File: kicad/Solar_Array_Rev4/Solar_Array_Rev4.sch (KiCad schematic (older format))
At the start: 7 parts

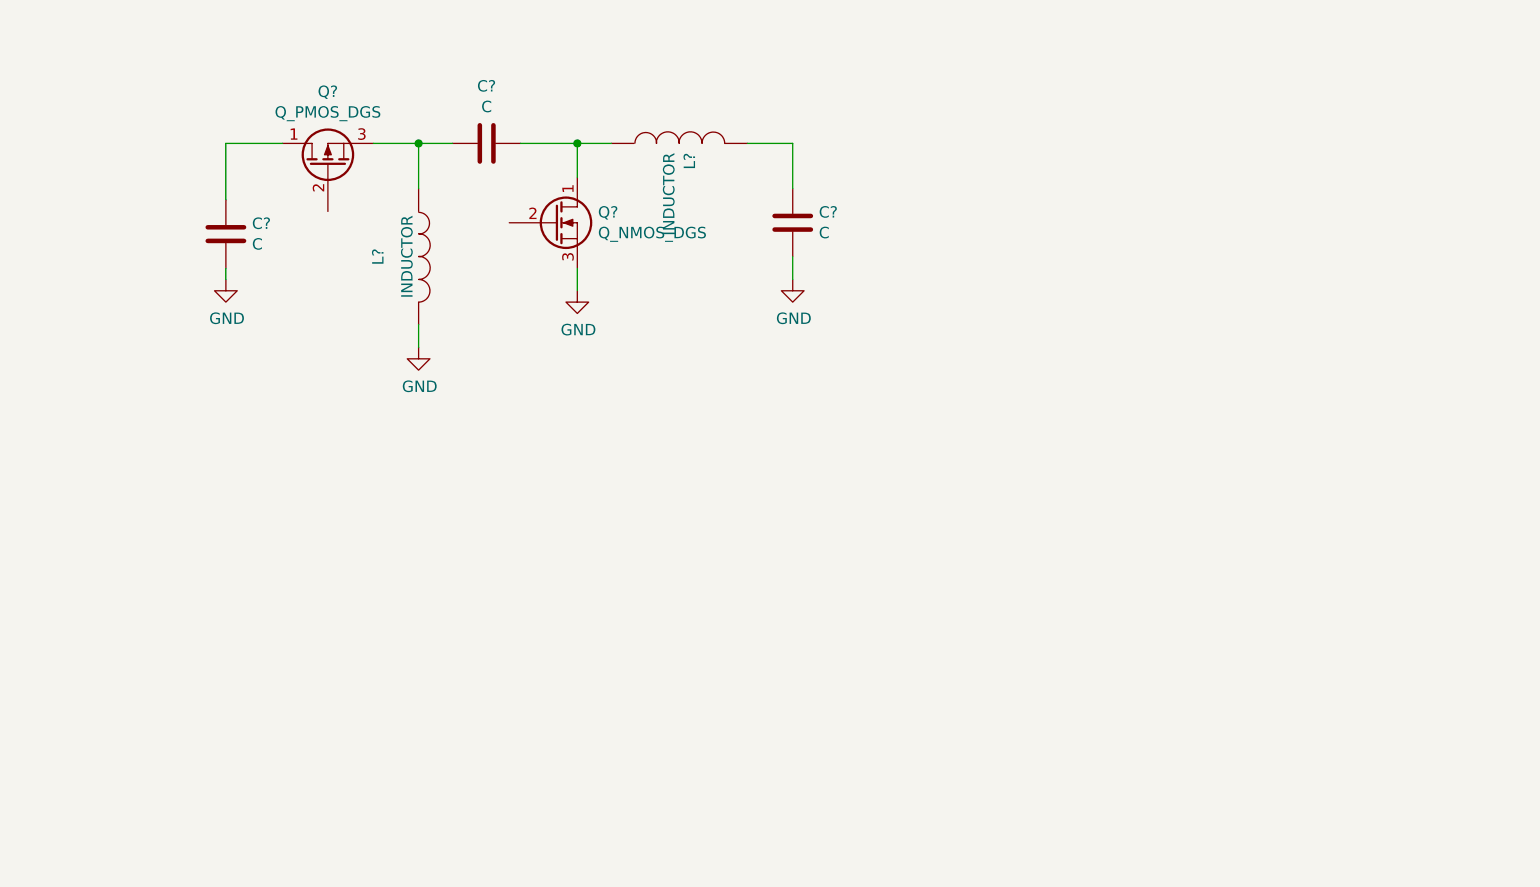
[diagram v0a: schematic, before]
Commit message: Created Schematics, Added Current Sense Circuitry -Created microcontroller schematic symbol -Created sense comparator schematic -Updated design with correct symbols -Added PV in/out -Calculated and selected --P-MOS --N-MOS --Check design docs for details
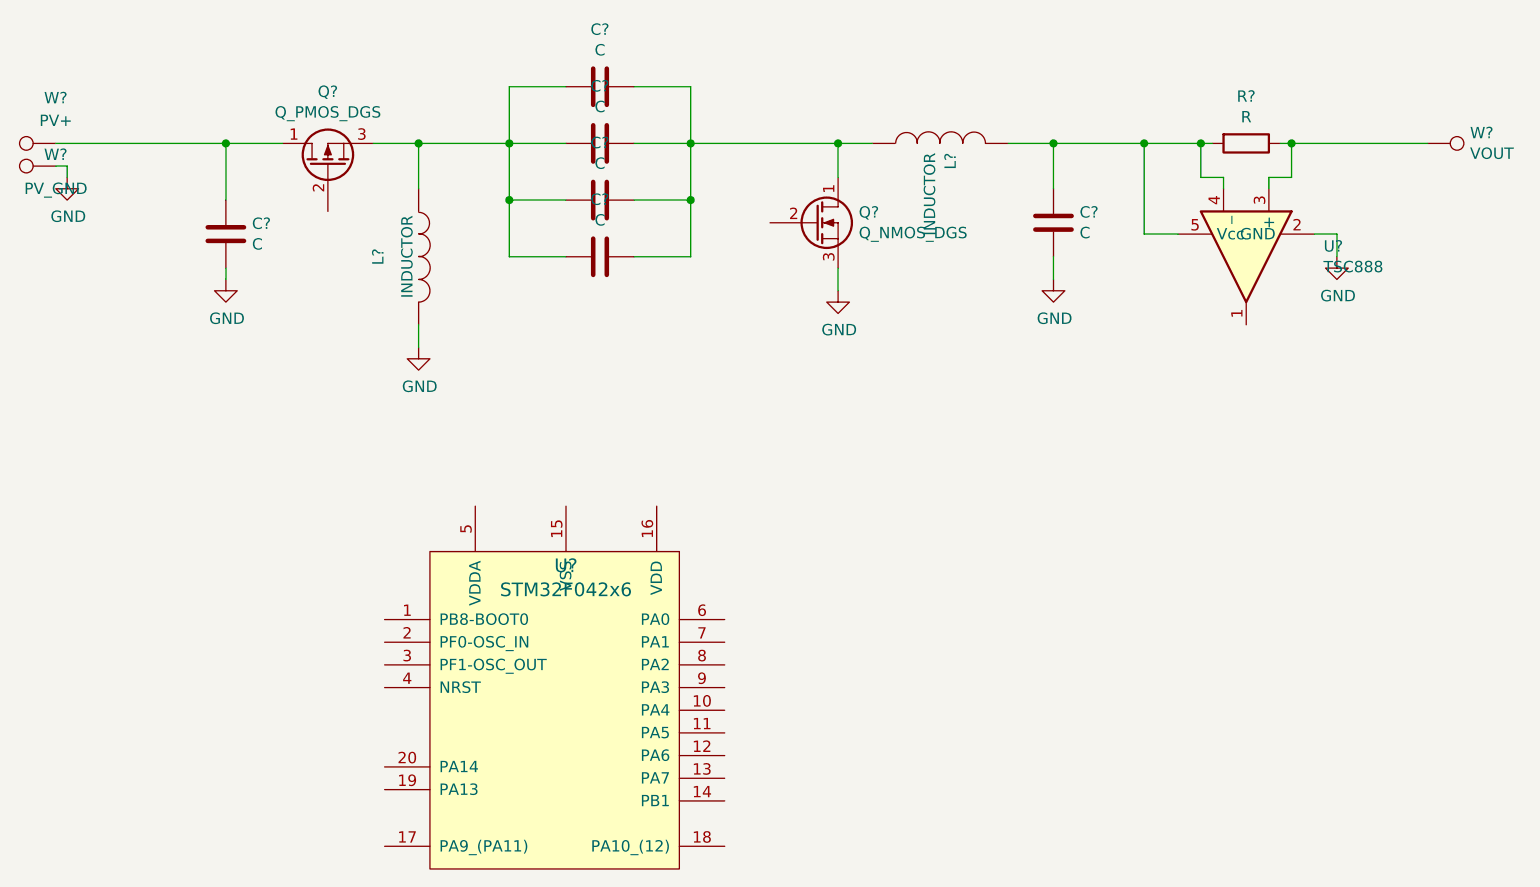
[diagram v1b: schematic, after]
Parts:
- added C? (x3): C, symbol C
- added R?: R, symbol R
- added U?: STM32F042x6, symbol STM32F042x6
- added U?: TSC888, symbol TSC888
- added W?: PV+, symbol TEST_1P
- added W?: PV_GND, symbol TEST_1P
- added W?: VOUT, symbol TEST_1P
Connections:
- net GND: now also U?.2 (GND), W?.1
- net at C?.1, L?.1, Q?.3 (S): now also C?.1, C?.1, C?.1
- net at C?.2, L?.1, Q?.1 (D): now also C?.2, C?.2, C?.2
- net at C?.1, L?.2: now also R?.2, U?.4 (_), U?.5 (Vcc)
- net at C?.1, Q?.1 (D): now also W?.1
- new net: R?.1, U?.3 (+), W?.1
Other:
- moved on the sheet: C?, L?, Q?

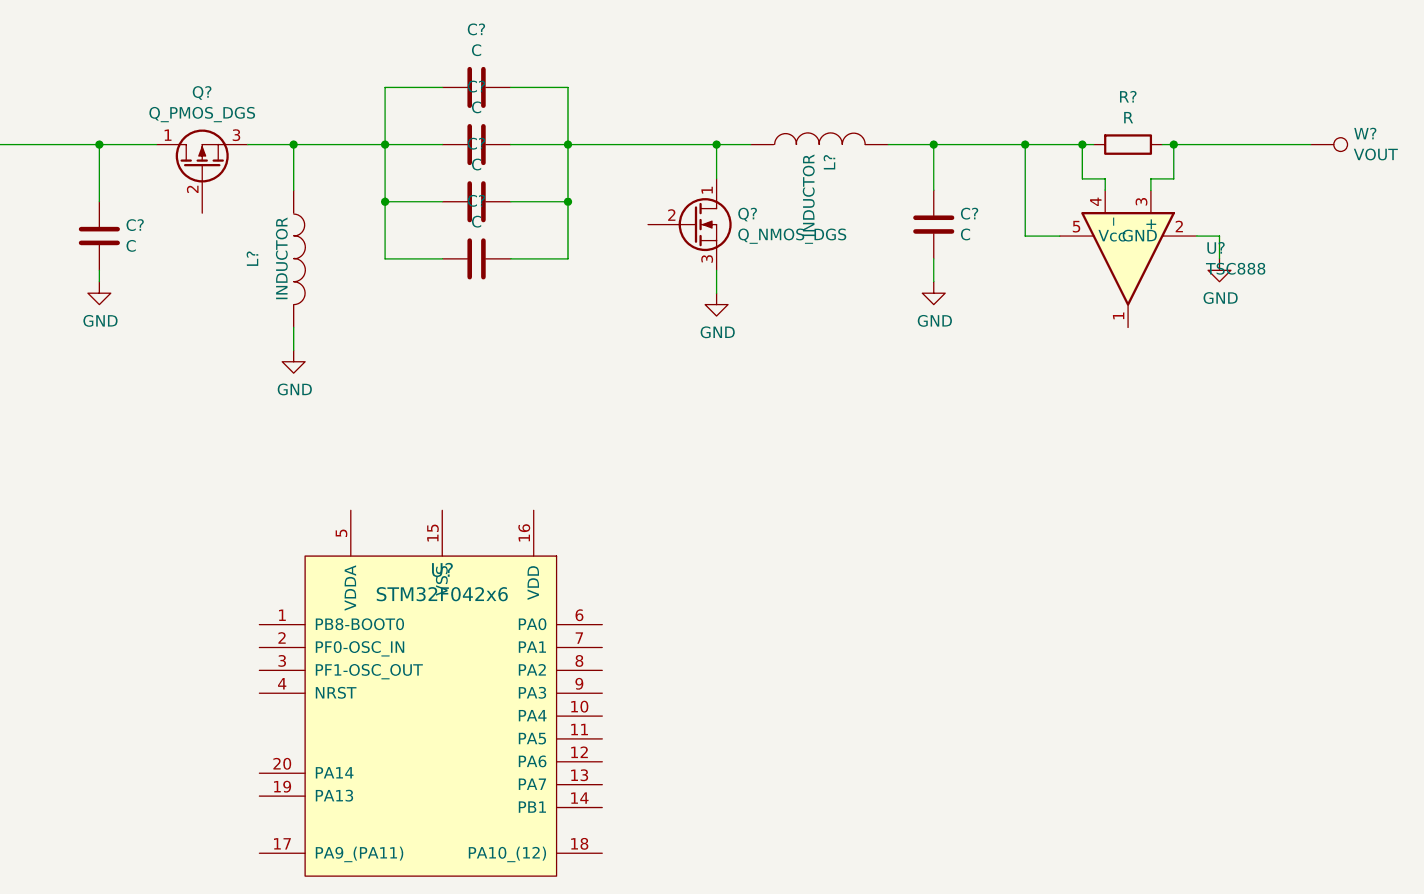
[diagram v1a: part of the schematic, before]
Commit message: Assigned Pin functions to ST microcontroller. -Found CAN TX/RX and assigned. -Found ADC in's for voltage/current sense. -Found TIM1 chn 1/3 for PWM control
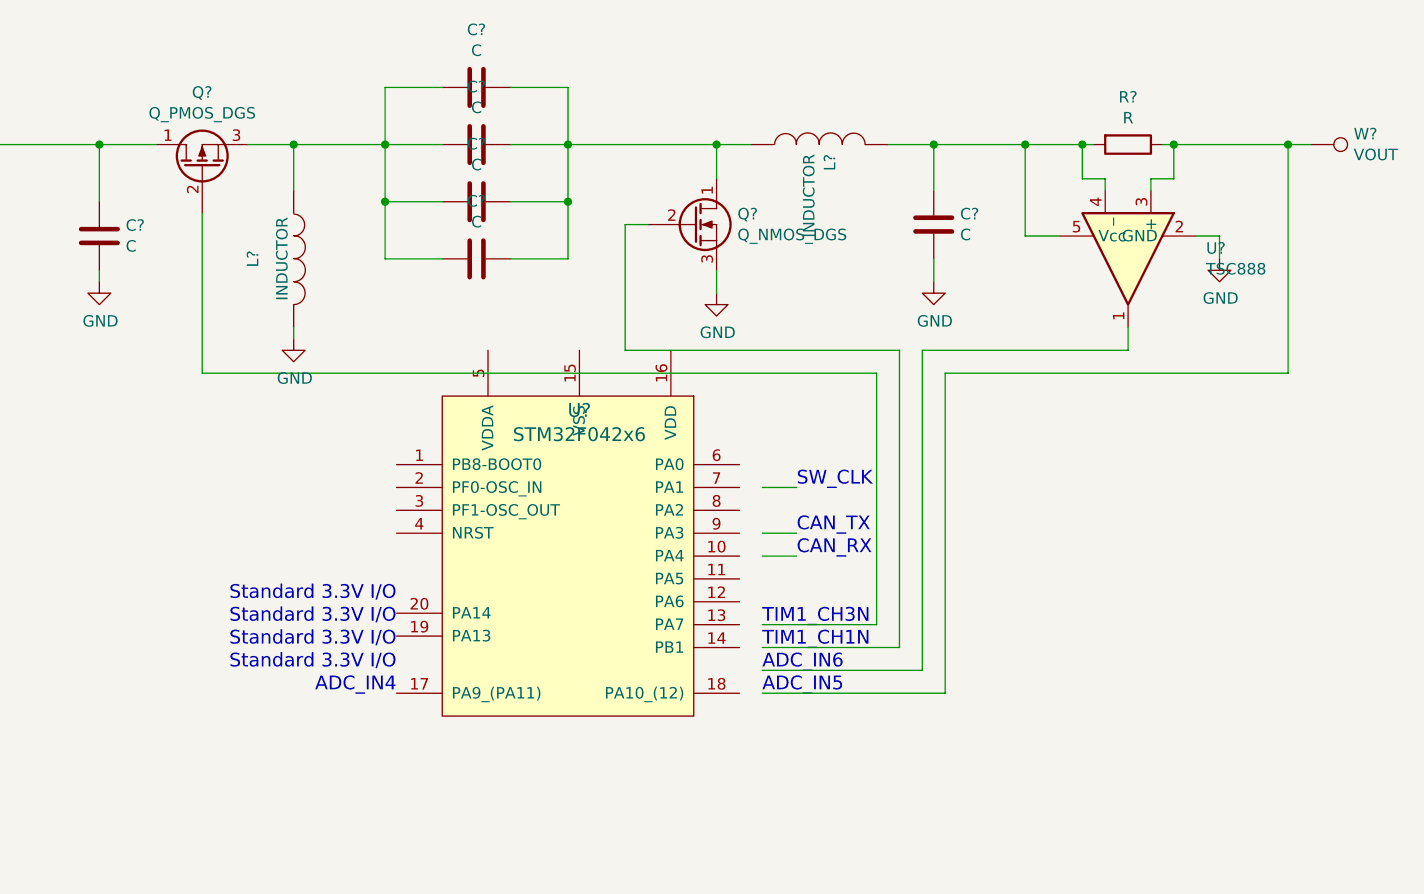
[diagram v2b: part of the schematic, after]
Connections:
- wire segments 33 -> 53
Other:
- note added: "ADC_IN4"
- note added: "ADC_IN5"
- note added: "ADC_IN6"
- note added: "CAN_RX"
- note added: "CAN_TX"
- note added: "SW_CLK"
- note added: "Standard 3.3V I/O"
- note added: "TIM1_CH1N"
- note added: "TIM1_CH3N"
- moved on the sheet: U?
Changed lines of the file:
@@
 L GND #PWR?
 U 1 1 57427E8E
-P 3550 3350
-F 0 "#PWR?" H 3550 3100 50  0001 C CNN
-F 1 "GND" H 3555 3177 50  0000 C CNN
-F 2 "" H 3550 3350 50  0000 C CNN
-F 3 "" H 3550 3350 50  0000 C CNN
-	1    3550 3350
+P 3550 3300
+F 0 "#PWR?" H 3550 3050 50  0001 C CNN
+F 1 "GND" H 3555 3127 50  0000 C CNN
+F 2 "" H 3550 3300 50  0000 C CNN
+F 3 "" H 3550 3300 50  0000 C CNN
+	1    3550 3300
 	1    0    0    -1
 $EndComp
@@
 L STM32F042x6 U?
 U 1 1 5748B95F
-P 4200 5100
-F 0 "U?" H 4200 5887 60  0000 C CNN
-F 1 "STM32F042x6" H 4200 5781 60  0000 C CNN
-F 2 "" H 4200 5100 60  0001 C CNN
-F 3 "" H 4200 5100 60  0001 C CNN
-	1    4200 5100
+P 4800 4400
+F 0 "U?" H 4800 5187 60  0000 C CNN
+F 1 "STM32F042x6" H 4800 5081 60  0000 C CNN
+F 2 "" H 4800 4400 60  0001 C CNN
+F 3 "" H 4800 4400 60  0001 C CNN
+	1    4800 4400
 	1    0    0    -1
 $EndComp
@@
 	2700 3000 2700 3050
 Wire Wire Line
-	3550 3250 3550 3350
-Wire Wire Line
 	5400 3000 5400 3100
 Wire Wire Line
@@
 	0    1    1    0
 $EndComp
+Connection ~ 7900 2450
+Wire Wire Line
+	5600 4250 5750 4250
+Wire Wire Line
+	5600 4150 5750 4150
+Text Notes 5750 4150 0    60   ~ 0
+CAN_TX
+Text Notes 5750 4250 0    60   ~ 0
+CAN_RX
+Text Notes 5750 3950 0    60   ~ 0
+SW_CLK
+Wire Wire Line
+	5600 3950 5750 3950
+Text Notes 4000 4450 2    60   ~ 0
+Standard 3.3V I/O
+Text Notes 4000 4550 2    60   ~ 0
+Standard 3.3V I/O
+Text Notes 4000 4650 2    60   ~ 0
+Standard 3.3V I/O
+Text Notes 4000 4750 2    60   ~ 0
+Standard 3.3V I/O
+Text Notes 4000 4850 2    60   ~ 0
+ADC_IN4
+Text Notes 5600 4650 0    60   ~ 0
+TIM1_CH1N
+Text Notes 5600 4550 0    60   ~ 0
+TIM1_CH3N
+Text Notes 5600 4850 0    60   ~ 0
+ADC_IN5
+Wire Wire Line
+	5600 4650 6200 4650
+Wire Wire Line
+	6200 4650 6200 3350
+Wire Wire Line
+	6200 3350 5000 3350
+Wire Wire Line
+	5000 3350 5000 2800
+Wire Wire Line
+	5000 2800 5100 2800
+Wire Wire Line
+	5600 4550 6100 4550
+Wire Wire Line
+	6100 4550 6100 3450
+Wire Wire Line
+	6100 3450 3150 3450
+Wire Wire Line
+	3150 3450 3150 2750
+Wire Wire Line
+	3550 3250 3550 3300
+Text Notes 5600 4750 0    60   ~ 0
+ADC_IN6
+Wire Wire Line
+	6300 4750 6300 3350
+Wire Wire Line
+	6300 3350 7200 3350
+Wire Wire Line
+	6300 4750 5600 4750
+Wire Wire Line
+	7200 3350 7200 3250
+Wire Wire Line
+	5600 4850 6400 4850
+Wire Wire Line
+	6400 4850 6400 3450
+Wire Wire Line
+	6400 3450 7900 3450
+Wire Wire Line
+	7900 3450 7900 2450
 $EndSCHEMATC

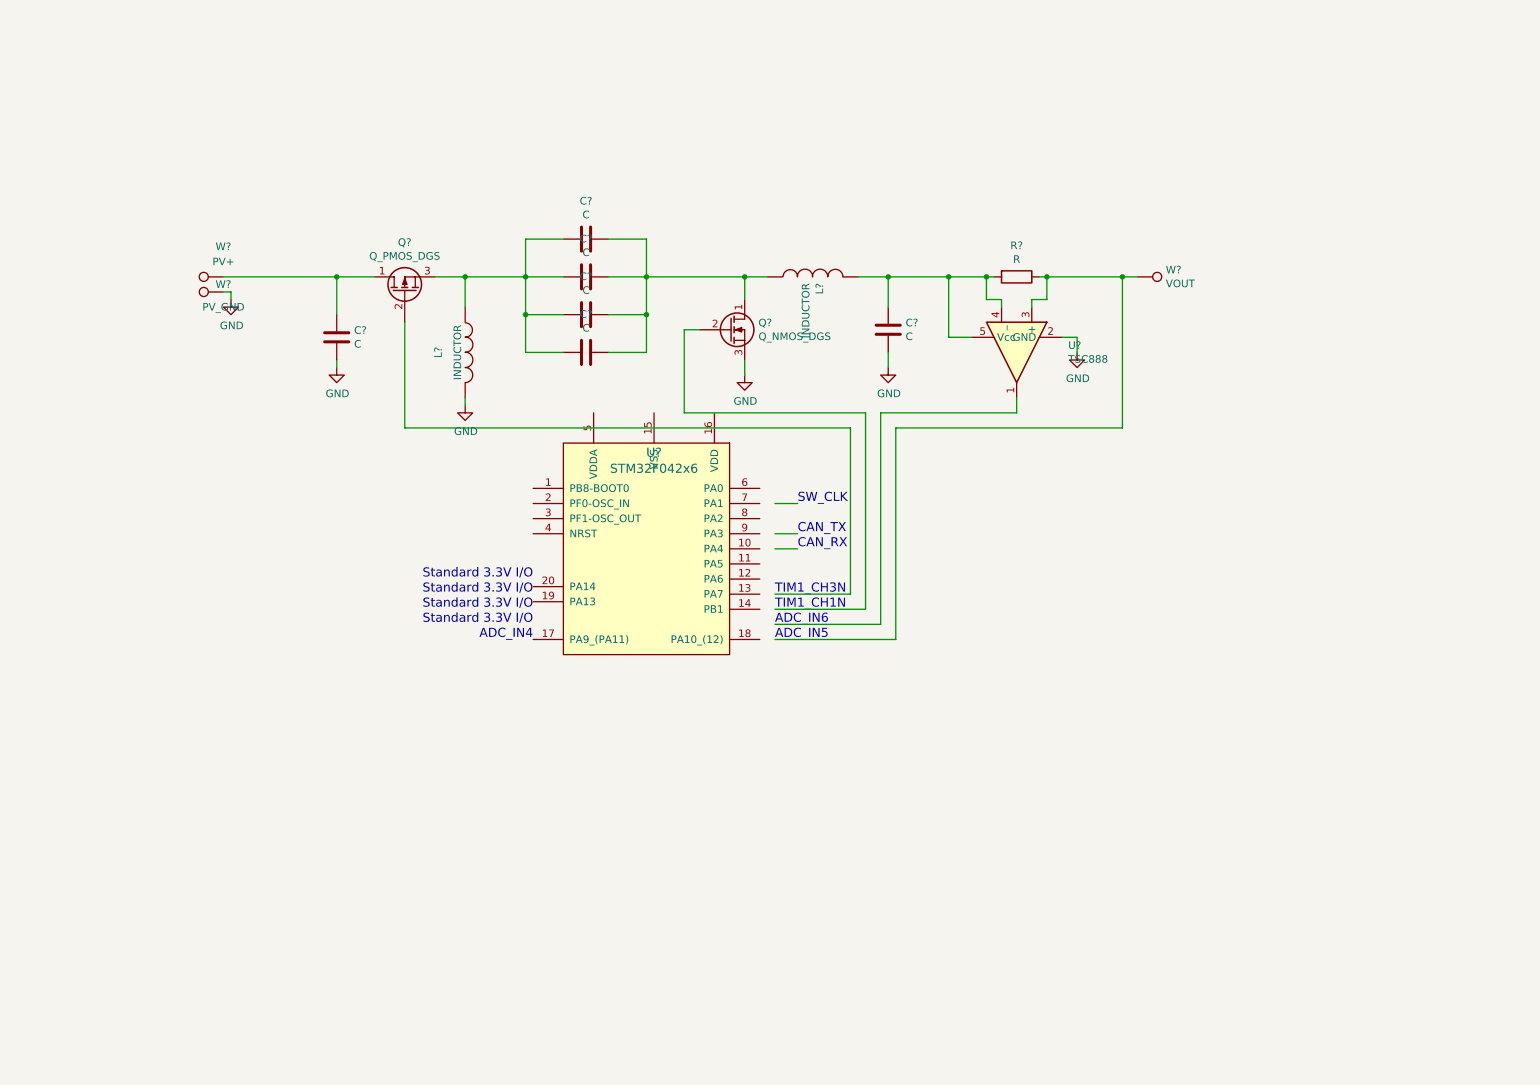
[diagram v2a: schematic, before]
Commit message: Included footrpints for SWD and CAN Transciever
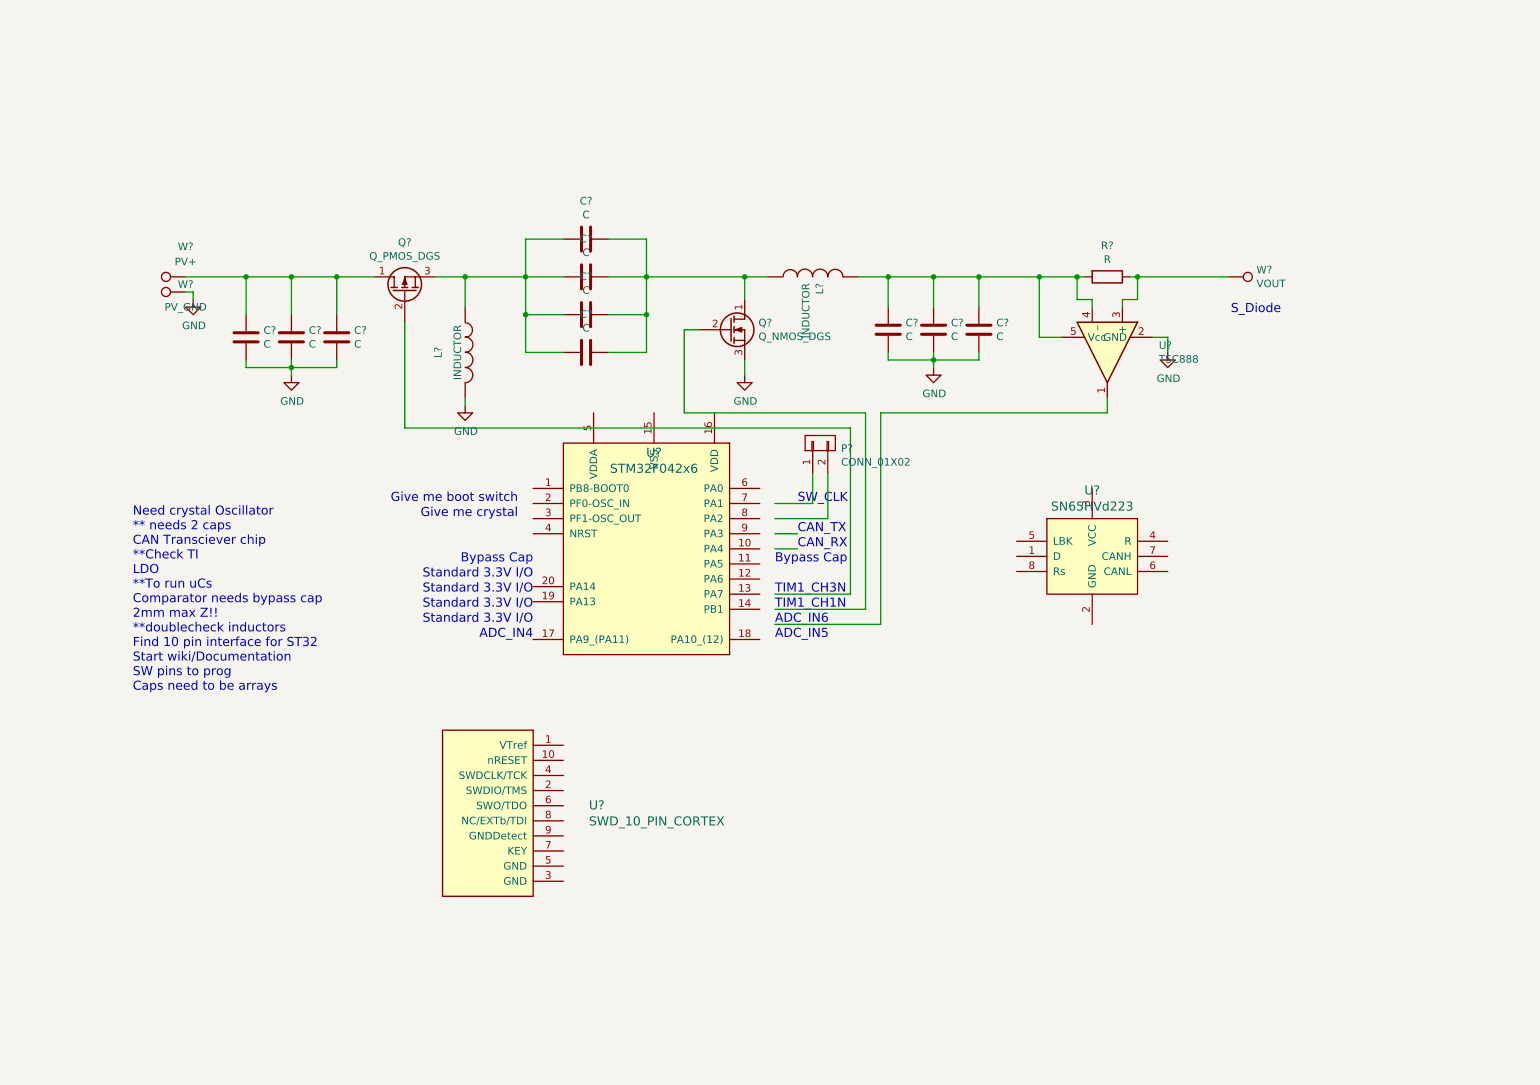
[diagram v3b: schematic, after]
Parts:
- added C? (x4): C, symbol C
- added P?: CONN_01X02, symbol CONN_01X02
- added U?: SN65HVd223, symbol SN65HVd223
- added U?: SWD_10_PIN_CORTEX, symbol SWD_10_PIN_CORTEX
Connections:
- wire segments 53 -> 62
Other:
- note added: "Bypass Cap"
- note added: "Give me boot switch"
- note added: "Give me crystal\n"
- note added: "Need crystal Oscillator\n** needs 2 caps\nCAN Transciever chip\n**Check TI\nLDO\n**To run uCs\nComparator needs bypass cap\n2mm max Z!!\n**doublecheck inductors\nFind 10 pin interface for ST32\nStart wiki/Documentation\nSW pins to prog\nCaps need to be arrays"
- note added: "S_Diode"
- moved on the sheet: R?, U?, W?
